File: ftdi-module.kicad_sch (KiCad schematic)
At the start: 58 parts, among them U1 AP62301_TSOT, U2 FT4232H_VQFN, U3 AP62301_TSOT, Y1 Resonator_12MHz_ABM8G

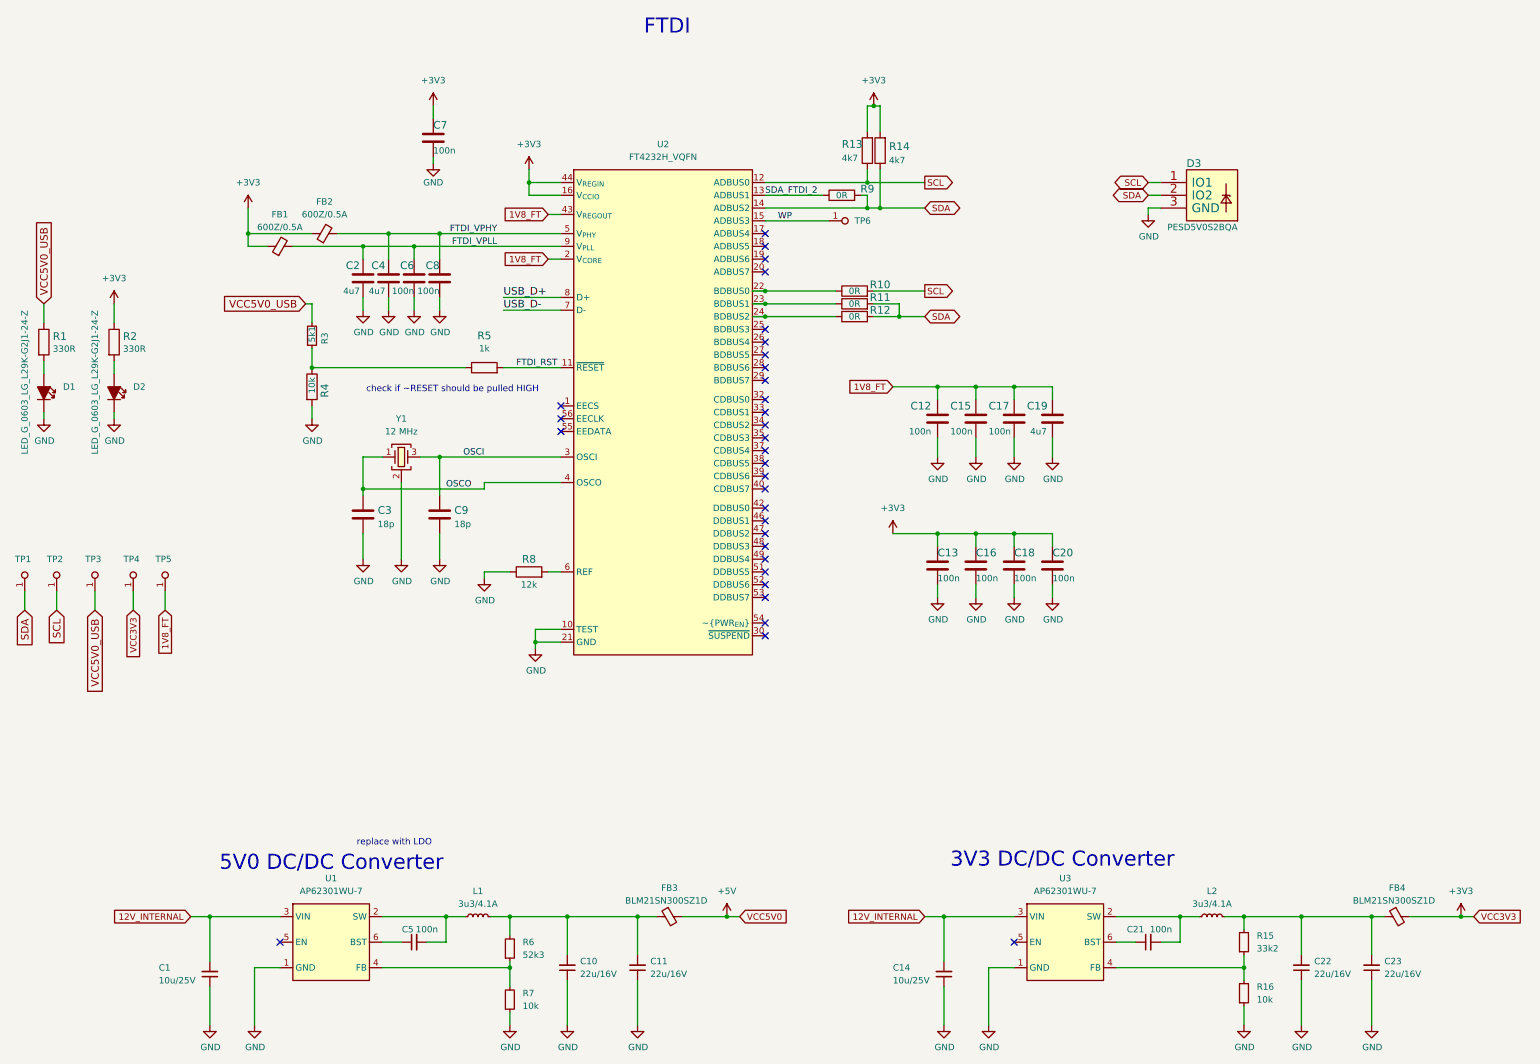
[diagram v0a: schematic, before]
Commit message: Repleace non standard components in connectors and ftdi and power
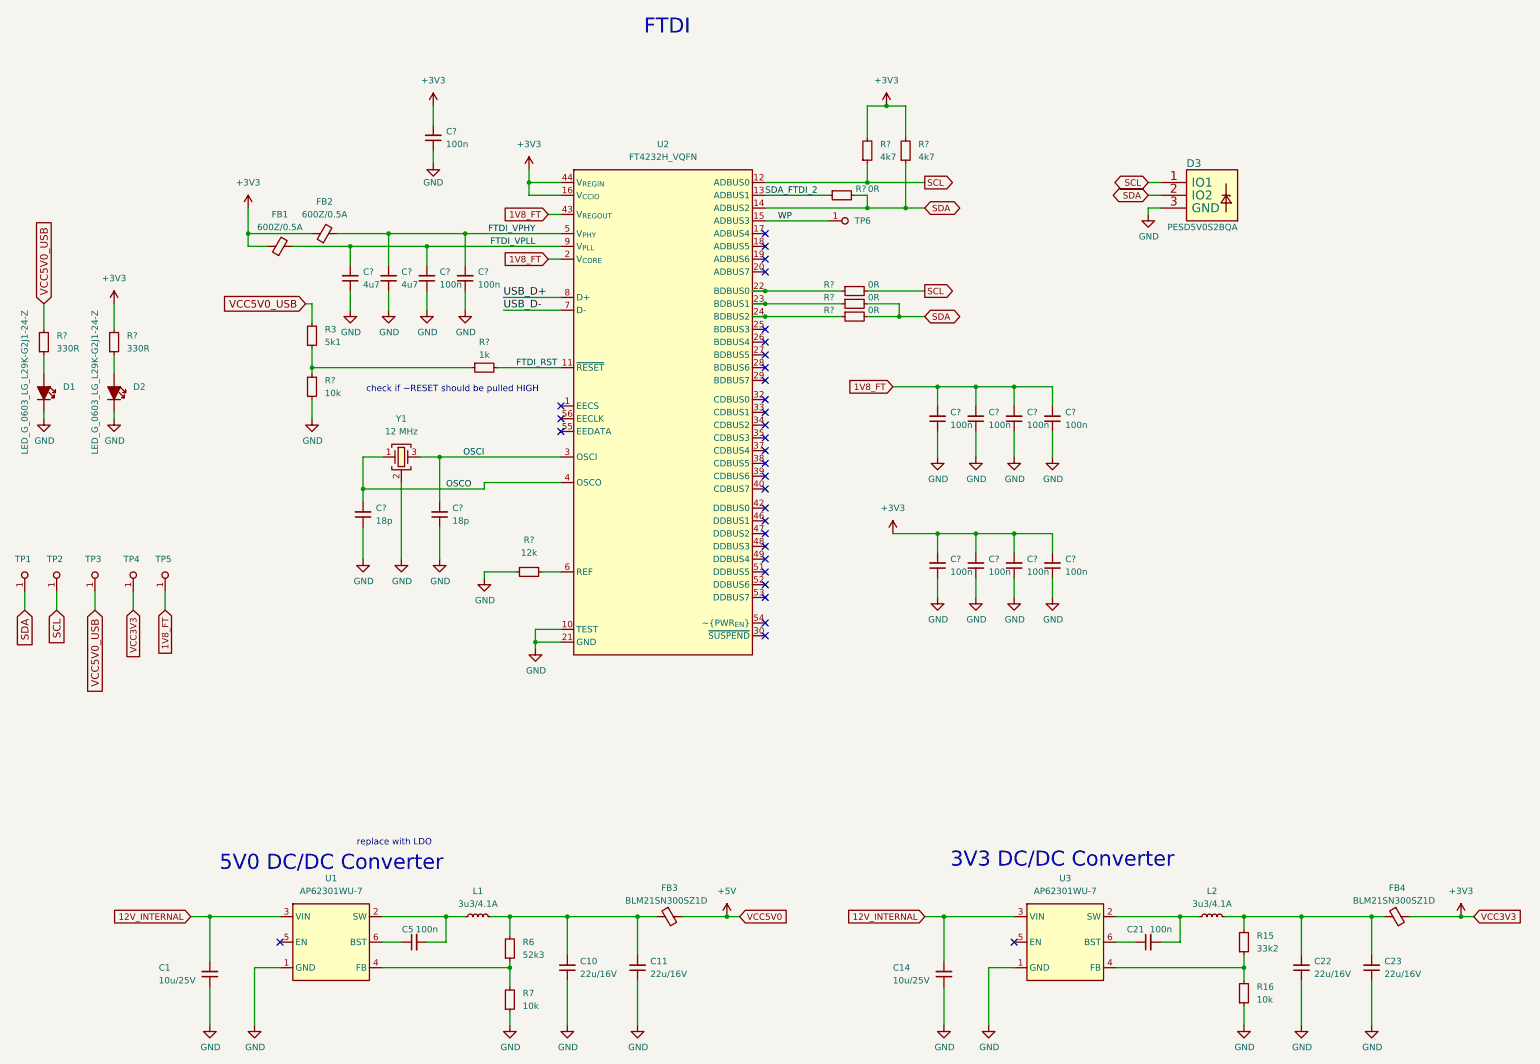
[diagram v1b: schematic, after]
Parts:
- removed C12, C13, C15, C16, C17, C18, C20, C6, C7, C8: C_100n_0402, antmicro-footprints:C_0402_1005Metric, symbol antmicroCapacitors0402:C_100n_0402
- removed C19, C2, C4: C_4u7_0402, antmicro-footprints:C_0402_1005Metric, symbol antmicroCapacitors0402:C_4u7_0402
- removed C3, C9: C_18p_0402, antmicro-footprints:0402-cap, symbol antmicroCapacitors0402:C_18p_0402
- removed R1, R2: R_330R_0402, antmicro-footprints:R_0402_1005Metric, symbol antmicroResistors0402:R_330R_0402
- removed R10, R11, R12, R9: R_0R_0603, antmicro-footprints:R_0603_1608Metric, symbol antmicroResistors0603:R_0R_0603
- removed R13, R14: R_4k7_0402, antmicro-footprints:R_0402_1005Metric, symbol antmicroResistors0402:R_4k7_0402
- removed R4: R_10k_0402, antmicro-footprints:R_0402_1005Metric, symbol antmicroResistors0402:R_10k_0402
- removed R5: R_1k_0402, antmicro-footprints:R_0402_1005Metric, symbol antmicroResistors0402:R_1k_0402
- removed R8: R_12k_0402, antmicro-footprints:R_0402_1005Metric, symbol antmicroResistors0402:R_12k_0402
- added C? (x11): C_100n_0402, antmicro-footprints:C_0402_1005Metric, symbol antmicroCapacitors0402:C_100n_0402
- added C? (x2): C_4u7_0402, antmicro-footprints:C_0402_1005Metric, symbol antmicroCapacitors0402:C_4u7_0402
- added C? (x2): C_18p_0402, antmicro-footprints:C_0402_1005Metric, symbol antmicroCapacitors0402:C_18p_0402
- added R?: R_10k_0402, antmicro-footprints:R_0402_1005Metric, symbol antmicroResistors0402:R_10k_0402
- added R? (x2): R_330R_0402, antmicro-footprints:R_0402_1005Metric, symbol antmicroResistors0402:R_330R_0402
- added R?: R_12k_0402, antmicro-footprints:R_0402_1005Metric, symbol antmicroResistors0402:R_12k_0402
- added R? (x4): R_0R_0402, antmicro-footprints:R_0402_1005Metric, symbol antmicroResistors0402:R_0R_0402
- added R? (x2): R_4k7_0402, antmicro-footprints:R_0402_1005Metric, symbol antmicroResistors0402:R_4k7_0402
- added R?: R_1k_0402, antmicro-footprints:R_0402_1005Metric, symbol antmicroResistors0402:R_1k_0402
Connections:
- net +3V3: now also C?.2, C?.2, C?.2, C?.2, C?.2, R?.2, R?.2, R?.2
- net 1V8_FT: now also C?.2, C?.2, C?.2, C?.2
- net FTDI_RST: now also R?.2
- net FTDI_VPHY: now also C?.2, C?.2
- net FTDI_VPLL: now also C?.2, C?.2
- net GND: now also C?.1, C?.1, C?.1, C?.1, C?.1, C?.1, C?.1, C?.1, C?.1, C?.1, C?.1, C?.1, C?.1, C?.1, C?.1, R?.1, R?.1
- net OSCI: now also C?.2
- net OSCO: now also C?.2
- net SCL: now also R?.1, R?.2
- net SDA: now also R?.1, R?.2, R?.2, R?.2
- net SDA_FTDI_2: now also R?.1
- net VCC5V0_USB: now also R?.2
- net at D1.1: now also R?.1
- net at R3.1: now also R?.1, R?.2
- net at U2.22 (BDBUS0): now also R?.1
- net at U2.23 (BDBUS1): now also R?.1
- net at U2.24 (BDBUS2): now also R?.1
- net at U2.6 (REF): now also R?.2
- net at D2.1: now also R?.1

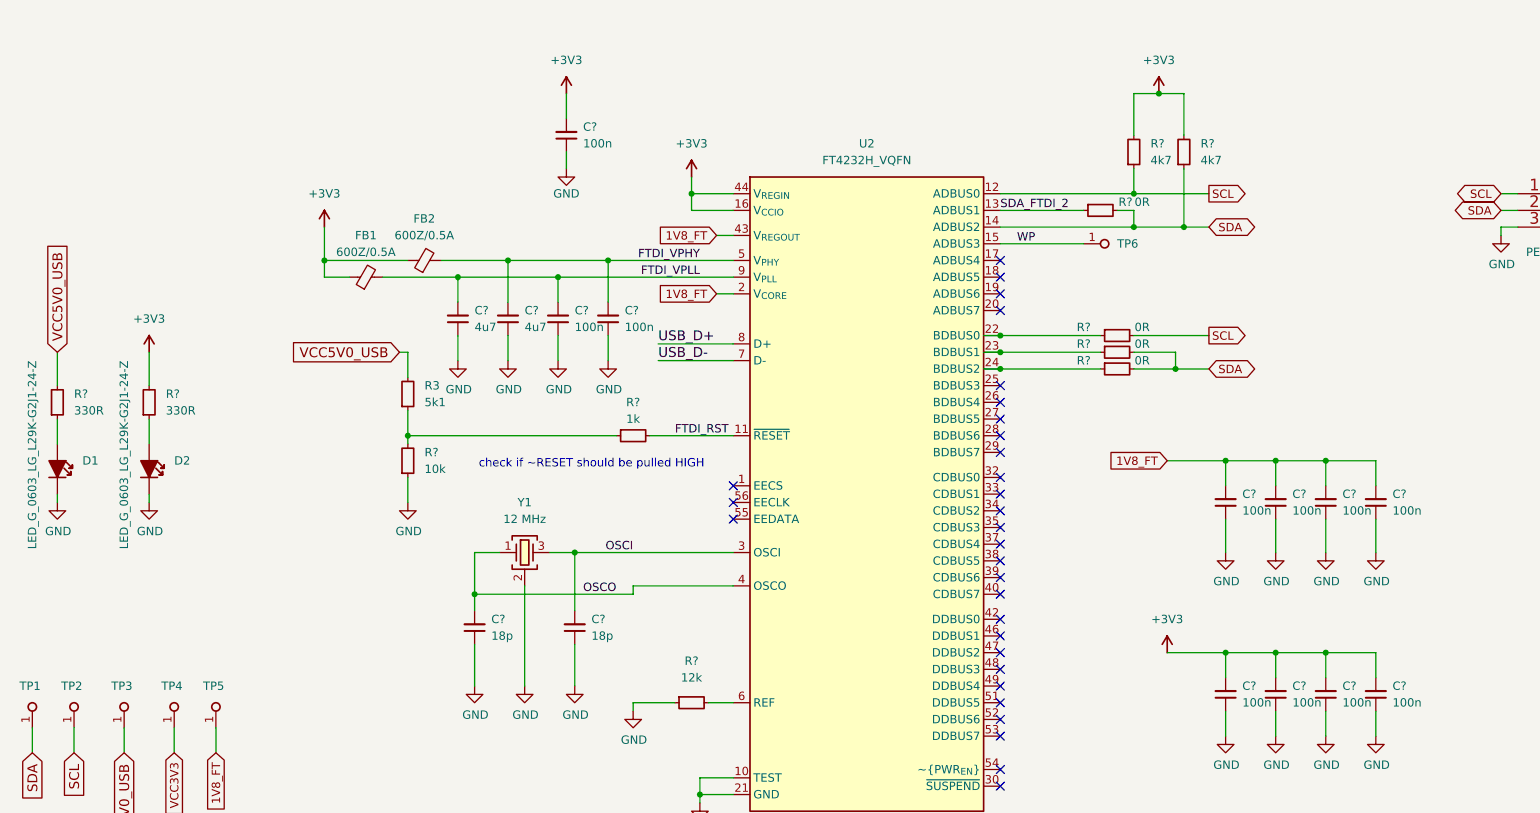
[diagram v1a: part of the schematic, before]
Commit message: Standarize mechanicals and output control
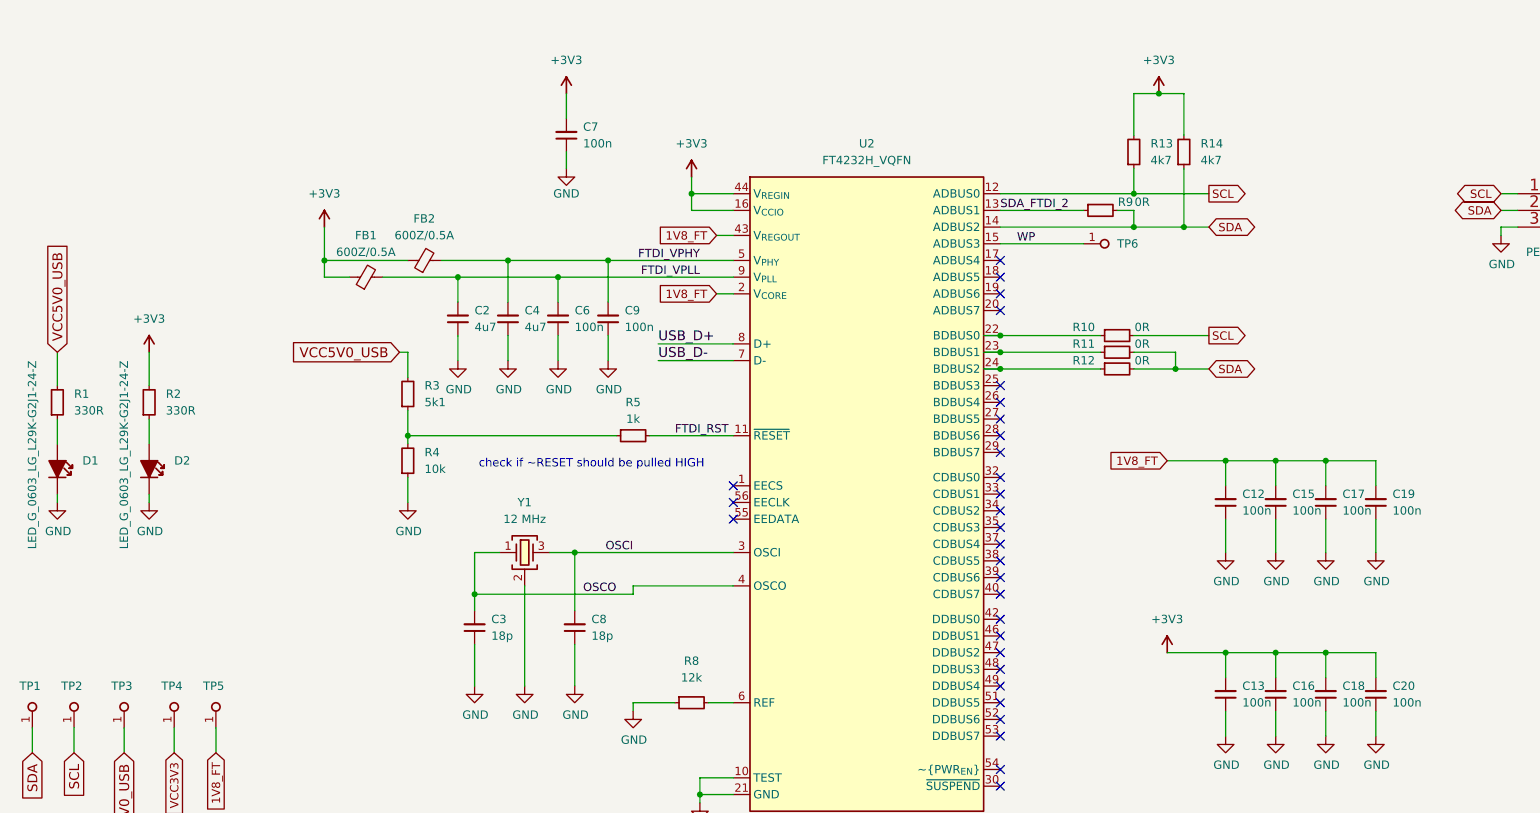
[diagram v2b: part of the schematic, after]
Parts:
- gave numbers to parts that had none: 26

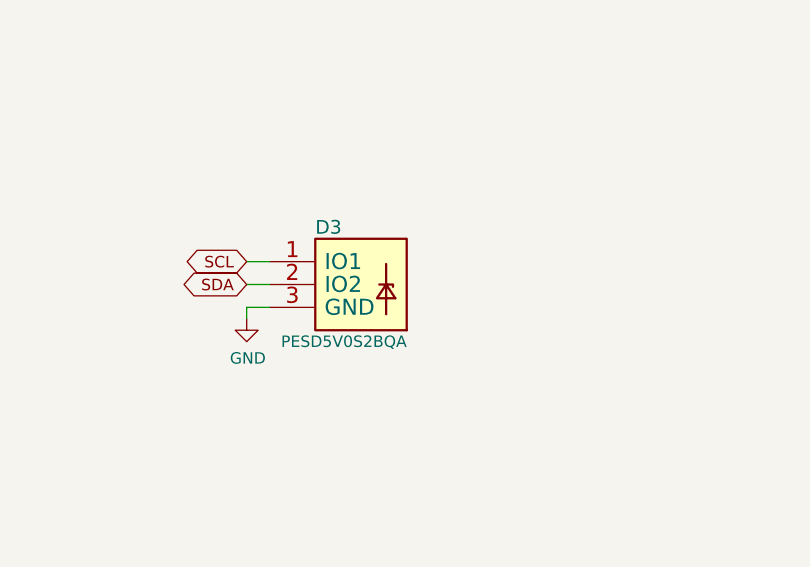
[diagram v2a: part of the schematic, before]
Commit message: 2nd batch of standardization of schematic
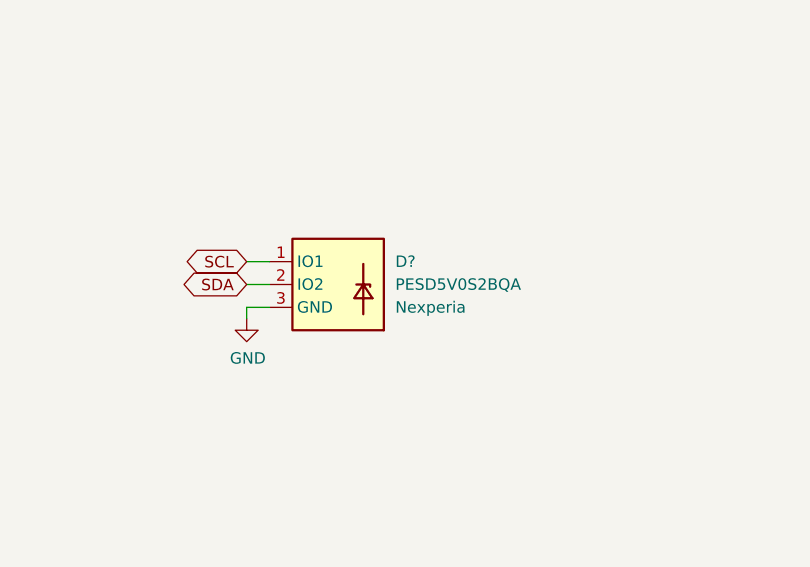
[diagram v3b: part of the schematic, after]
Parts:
- removed D3: PESD5V0S2BQA, antmicro-footprints:TPD2E009DRTR, symbol antmicroTVSDiodes:PESD5V0S2BQA
- added D?: PESD5V0S2BQA, antmicro-footprints:TPD2E009DRTR, symbol antmicroTVSDiodes:PESD5V0S2BQA
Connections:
- net GND: now also D?.3 (GND)
- net SCL: now also D?.1 (IO1)
- net SDA: now also D?.2 (IO2)
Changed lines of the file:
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@@
     (pin "1")
+  )
+  (symbol (lib_name "PESD5V0S2BQA_1") (lib_id "antmicroTVSDiodes:PESD5V0S2BQA") (at 255.27 53.34 0) (unit 1)
+    (in_bom yes) (on_board yes) (fields_autoplaced)
+    (property "Reference" "D?" (id 0) (at 269.24 53.3399 0)
+      (effects (font (size 1.27 1.27) (thickness 0.15)) (justify left))
+    )
+    (property "Value" "PESD5V0S2BQA" (id 1) (at 283.21 63.5 0)
+      (effects (font (size 1.27 1.27) (thickness 0.15)) (justify left bottom) hide)
+    )
+    (property "Footprint" "antmicro-footprints:TPD2E009DRTR" (id 2) (at 283.21 66.04 0)
+      (effects (font (size 1.27 1.27) (thickness 0.15)) (justify left bottom) hide)
+    )
+    (property "Datasheet" "https://4donline.ihs.com/images/VipMasterIC/IC/NEXP/NEXP-S-A0003105620/NEXP-S-A0003107857-1.pdf?hkey=6D3A4C79FDBF58556ACFDE234799DDF0" (id 3) (at 283.21 68.58 0)
+      (effects (font (size 1.27 1.27) (thickness 0.15)) (justify left bottom) hide)
+    )
+    (property "MPN" "PESD5V0S2BQA" (id 4) (at 269.24 55.8799 0)
+      (effects (font (size 1.27 1.27) (thickness 0.15)) (justify left))
+    )
+    (property "Manufacturer" "Nexperia" (id 5) (at 269.24 58.4199 0)
+      (effects (font (size 1.27 1.27) (thickness 0.15)) (justify left))
+    )
+    (property "Author" "Antmicro" (id 6) (at 283.21 71.12 0)
+      (effects (font (size 1.27 1.27) (thickness 0.15)) (justify left bottom) hide)
+    )
+    (property "License" "Apache-2.0" (id 7) (at 283.21 73.66 0)
+      (effects (font (size 1.27 1.27) (thickness 0.15)) (justify left bottom) hide)
+    )
+    (pin "1")
+    (pin "2")
+    (pin "3")
   )
   (symbol (lib_name "C_4u7_0402_1") (lib_id "antmicroCapacitors0402:C_4u7_0402") (at 93.98 74.93 90) (unit 1)
@@
     (pin "2")
   )
-  (symbol (lib_id "antmicroTVSDiodes:PESD5V0S2BQA") (at 260.35 53.34 0) (unit 1)
-    (in_bom yes) (on_board yes)
-    (property "Reference" "D3" (id 0) (at 260.35 49.53 0)
-      (effects (font (size 1.524 1.524)) (justify left))
-    )
-    (property "Value" "PESD5V0S2BQA" (id 1) (at 252.73 68.58 90)
-      (effects (font (size 1.524 1.524)) (justify left bottom) hide)
-    )
-    (property "Footprint" "antmicro-footprints:TPD2E009DRTR" (id 2) (at 261.62 48.26 0)
-      (effects (font (size 1.524 1.524)) hide)
-    )
-    (property "Datasheet" "" (id 3) (at 260.35 53.34 0)
-      (effects (font (size 1.524 1.524)) hide)
-    )
-    (property "MPN" "PESD5V0S2BQA" (id 4) (at 256.54 62.23 0)
-      (effects (font (size 1.27 1.27)) (justify left))
-    )
-    (property "Manufacturer" "Nexperia" (id 5) (at 261.62 64.77 0)
-      (effects (font (size 1.27 1.27)) (justify left) hide)
-    )
-    (pin "1")
-    (pin "2")
-    (pin "3")
-  )
   (symbol (lib_id "antmicroResistors0402:R_52k3_0402") (at 125.73 208.28 90) (unit 1)

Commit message: Next batch of standardization
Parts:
- gave numbers to parts that had none: 1
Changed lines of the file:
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@@
   (symbol (lib_name "PESD5V0S2BQA_1") (lib_id "antmicroTVSDiodes:PESD5V0S2BQA") (at 255.27 53.34 0) (unit 1)
     (in_bom yes) (on_board yes) (fields_autoplaced)
-    (property "Reference" "D?" (id 0) (at 269.24 53.3399 0)
+    (property "Reference" "D3" (id 0) (at 269.24 53.3399 0)
       (effects (font (size 1.27 1.27) (thickness 0.15)) (justify left))
     )
